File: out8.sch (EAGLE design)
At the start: 38 parts, among them IC1 74HC595N, K301 S202S02, K302 S202S02, K303 S202S02, K304 S202S02, K305 S202S02, K306 S202S02, K307 S202S02, K308 S202S02

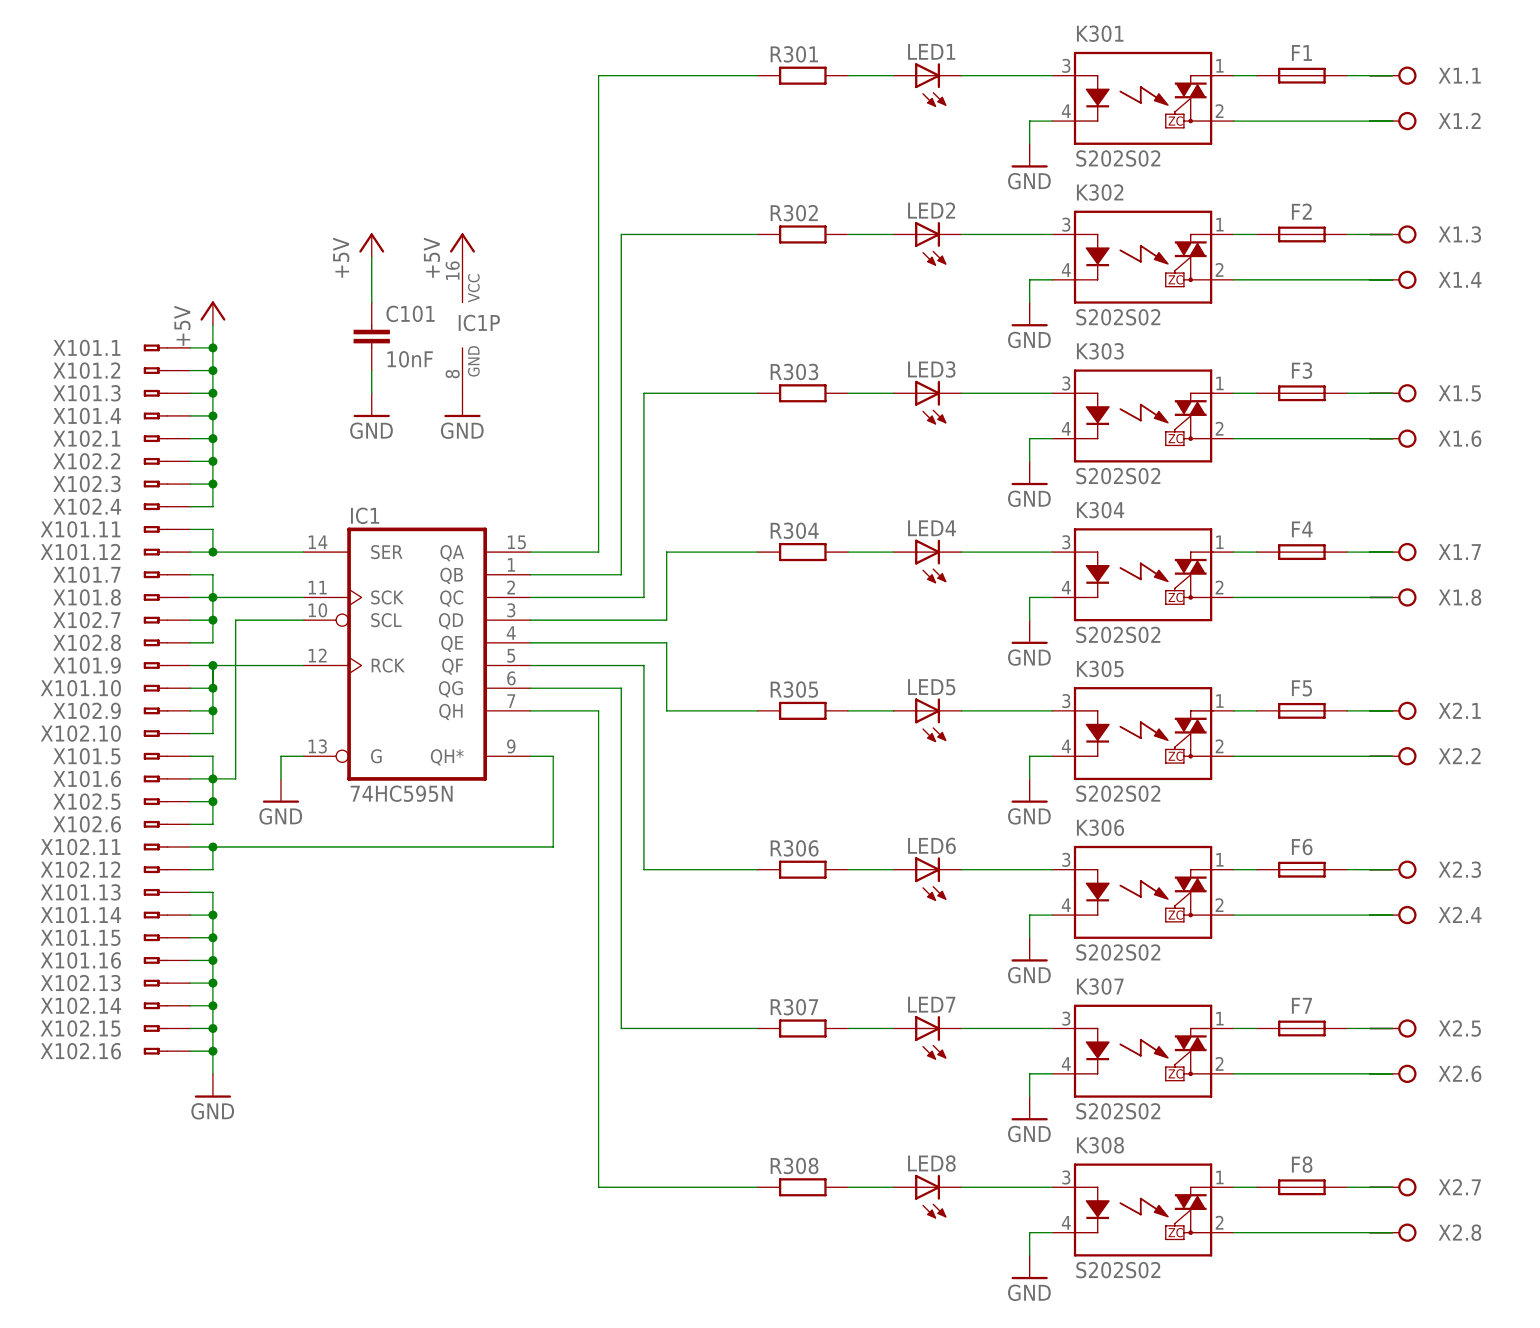
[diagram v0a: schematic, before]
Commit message: Boards beschriftet
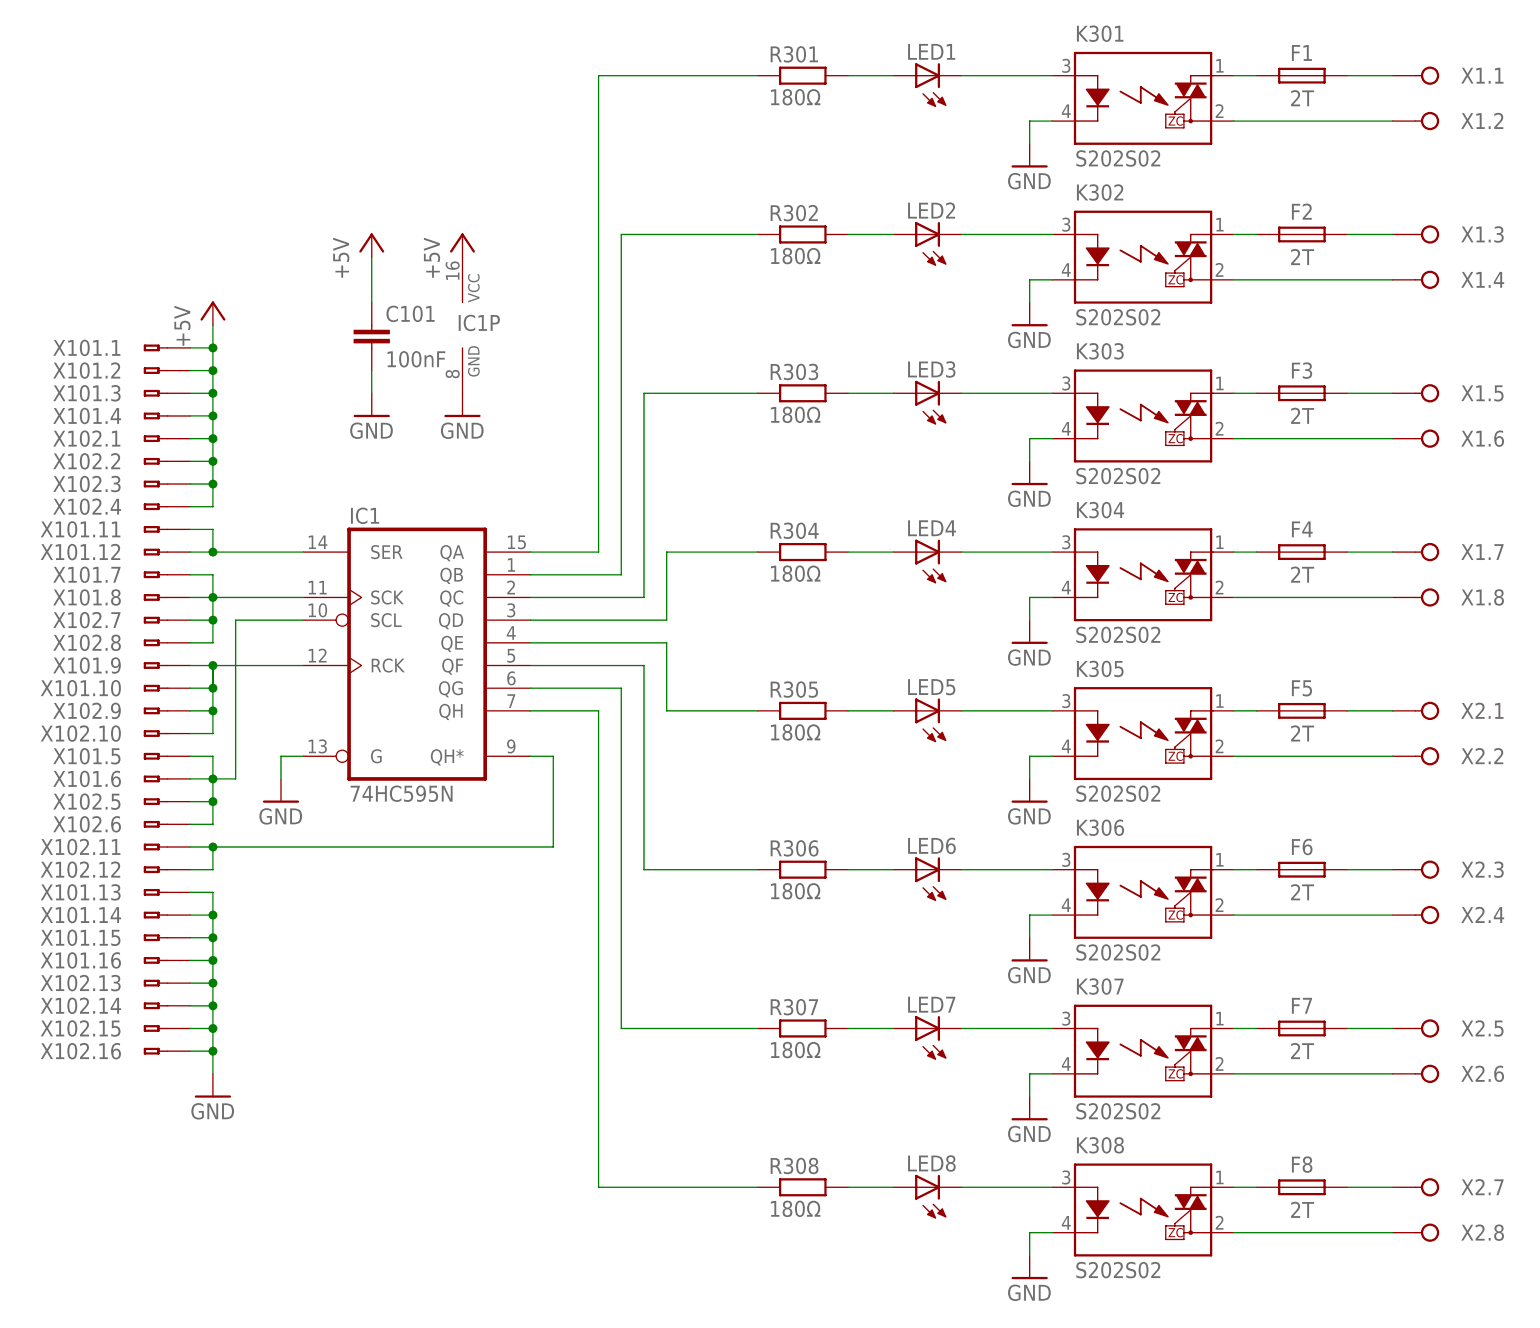
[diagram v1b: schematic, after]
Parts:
- C101: value 10nF -> 100nF
- F1, F2, F3, F4, F5, F6, F7, F8: value (none) -> 2T
- R301, R302, R303, R304, R305, R306, R307, R308: value (none) -> 180Ω
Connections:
- net N$10: no longer X1.1.B
- net N$11: no longer X1.2.B
- net N$13: no longer X1.3.B
- net N$14: no longer X1.4.B
- net N$16: no longer X1.5.B
- net N$25: no longer X1.6.B
- net N$27: no longer X1.7.B
- net N$28: no longer X1.8.B
- net N$30: no longer X2.1.B
- net N$31: no longer X2.2.B
- net N$33: no longer X2.3.B
- net N$34: no longer X2.4.B
- net N$36: no longer X2.5.B
- net N$37: no longer X2.6.B
- net N$39: no longer X2.7.B
- net N$40: no longer X2.8.B
